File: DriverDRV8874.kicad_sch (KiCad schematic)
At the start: 30 parts, among them J1 Conn_01x06, J2 Conn_01x06, U1 DRV8874PWPR, U11 Green LED, U12 Green LED, U2 DRV8874PWPR

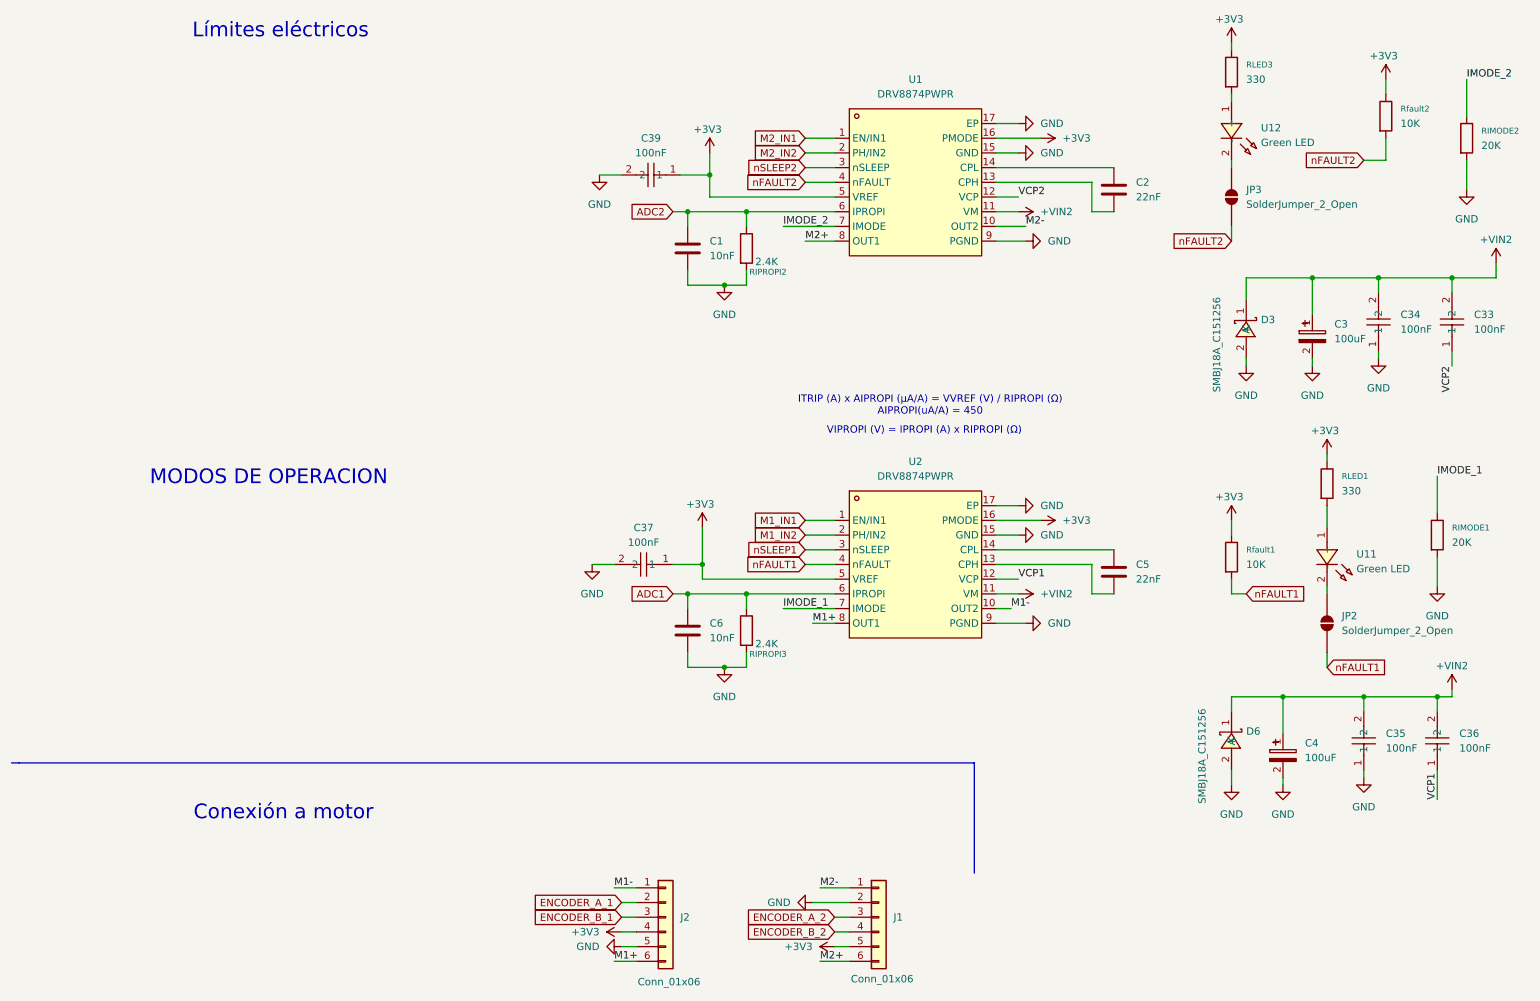
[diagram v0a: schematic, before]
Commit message: Primer Ruteo de PCB
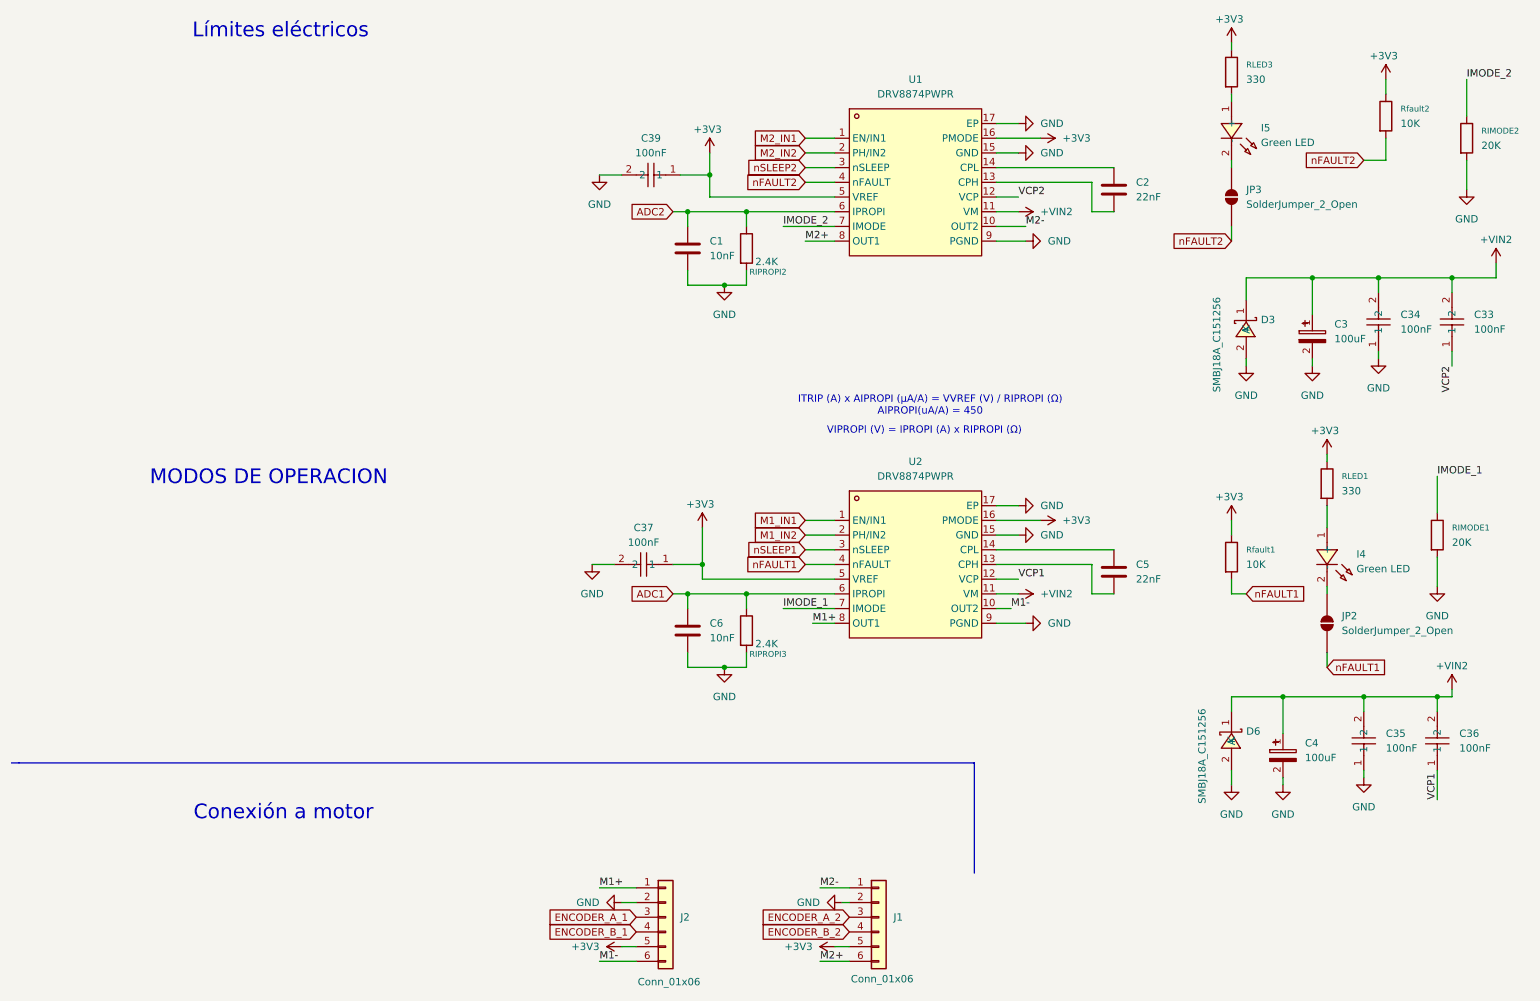
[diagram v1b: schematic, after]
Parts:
- C33, C34, C35, C36, C37, C39: footprint ARLISS-footprints:C0402 -> Capacitor_SMD:C_0402_1005Metric_Pad0.74x0.62mm_HandSolder
- renumbered U11 to I4, U12 to I5
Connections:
- net +3V3: now also J2.5 (Pin_5); no longer J2.4 (Pin_4)
- net ENCODER_A_1: now also J2.3 (Pin_3); no longer J2.2 (Pin_2)
- net ENCODER_B_1: now also J2.4 (Pin_4); no longer J2.3 (Pin_3)
- net GND: now also J2.2 (Pin_2); no longer J2.5 (Pin_5)
- net M1+: now also J2.1 (Pin_1); no longer J2.6 (Pin_6)
- net M1-: now also J2.6 (Pin_6); no longer J2.1 (Pin_1)

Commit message: Arreglos de esquemático
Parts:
- removed I4, I5: Green LED, ARLISS-footprints:LED0603-FD, symbol CANSAT_STM32_symbols:YLED0603G
- removed JP2, JP3: SolderJumper_2_Open, Jumper:SolderJumper-2_P1.3mm_Open_TrianglePad1.0x1.5mm, symbol Jumper:SolderJumper_2_Open
- removed RLED1, RLED3: 330, Resistor_SMD:R_0603_1608Metric_Pad0.98x0.95mm_HandSolder, symbol Device:R
- removed Rfault1, Rfault2: 10K, Resistor_SMD:R_0603_1608Metric_Pad0.98x0.95mm_HandSolder, symbol Device:R
- added LED4, LED5: D-R060306L3-KS2, Diode_SMD:D_0603_1608Metric_Pad1.05x0.95mm_HandSolder, symbol CANSAT_STM32_symbols:D-R060306L3-KS2
- added R15, R20: 1K, Resistor_SMD:R_0603_1608Metric_Pad0.98x0.95mm_HandSolder, symbol CANSAT_STM32_symbols:RC0603FR-071KL
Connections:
- net +3V3: now also R15.2, R20.2
- net nFAULT1: now also LED4.1 (-)
- net nFAULT2: now also LED5.1 (-)
- new net: LED4.2 (+), R20.1
- new net: LED5.2 (+), R15.1

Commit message: Arreglando footprints
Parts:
- C15: renamed from C37; footprint Capacitor_SMD:C_0402_1005Metric_Pad0.74x0.62mm_HandSolder -> Capacitor_SMD:C_0603_1608Metric_Pad1.08x0.95mm_HandSolder; Manufacturer CCTC(三环) -> (none)
- C16: renamed from C39; footprint Capacitor_SMD:C_0402_1005Metric_Pad0.74x0.62mm_HandSolder -> Capacitor_SMD:C_0603_1608Metric_Pad1.08x0.95mm_HandSolder; Manufacturer CCTC(三环) -> (none)
- C17: renamed from C1; footprint Capacitor_SMD:C_0402_1005Metric_Pad0.74x0.62mm_HandSolder -> Capacitor_SMD:C_0603_1608Metric_Pad1.08x0.95mm_HandSolder
- C18: renamed from C6; footprint Capacitor_SMD:CP_Elec_6.3x5.4 -> Capacitor_SMD:C_0603_1608Metric_Pad1.08x0.95mm_HandSolder
- C19: renamed from C2; footprint Capacitor_SMD:C_0402_1005Metric_Pad0.74x0.62mm_HandSolder -> Capacitor_SMD:C_0603_1608Metric_Pad1.08x0.95mm_HandSolder
- C20: renamed from C5; footprint Capacitor_SMD:C_0402_1005Metric_Pad0.74x0.62mm_HandSolder -> Capacitor_SMD:C_0603_1608Metric_Pad1.08x0.95mm_HandSolder
- C21: renamed from C4; Manufacturer Nichicon(尼吉康) -> (none)
- C22: renamed from C3; Manufacturer Nichicon(尼吉康) -> (none)
- C23: renamed from C35; footprint Capacitor_SMD:C_0402_1005Metric_Pad0.74x0.62mm_HandSolder -> Capacitor_SMD:C_0603_1608Metric_Pad1.08x0.95mm_HandSolder; Manufacturer CCTC(三环) -> (none)
- C24: renamed from C34; footprint Capacitor_SMD:C_0402_1005Metric_Pad0.74x0.62mm_HandSolder -> Capacitor_SMD:C_0603_1608Metric_Pad1.08x0.95mm_HandSolder; Manufacturer CCTC(三环) -> (none)
- C25: renamed from C36; footprint Capacitor_SMD:C_0402_1005Metric_Pad0.74x0.62mm_HandSolder -> Capacitor_SMD:C_0603_1608Metric_Pad1.08x0.95mm_HandSolder; Manufacturer CCTC(三环) -> (none)
- C26: renamed from C33; footprint Capacitor_SMD:C_0402_1005Metric_Pad0.74x0.62mm_HandSolder -> Capacitor_SMD:C_0603_1608Metric_Pad1.08x0.95mm_HandSolder; Manufacturer CCTC(三环) -> (none)
- D1: renamed from D6; Manufacturer Littelfuse(美国力特) -> (none)
- D2: renamed from D3; Manufacturer Littelfuse(美国力特) -> (none)
- LED2: renamed from LED4; Manufacturer ARKLED(方舟) -> (none)
- LED3: renamed from LED5; Manufacturer ARKLED(方舟) -> (none)
- R10: renamed from R15; Manufacturer YAGEO(国巨) -> (none)
- R9: renamed from R20; Manufacturer YAGEO(国巨) -> (none)
- U3: renamed from U1; Manufacturer TI(德州仪器) -> (none)
- U4: renamed from U2; Manufacturer TI(德州仪器) -> (none)
- renumbered J2 to J1, J1 to J2, RIPROPI2 to RIPROPI1, RIPROPI3 to RIPROPI2
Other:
- company: (none) -> TOMEK TEAM
